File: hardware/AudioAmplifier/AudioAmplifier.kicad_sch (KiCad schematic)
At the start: 7 parts, among them J1 Screw_Terminal_01x02, U1 LM386

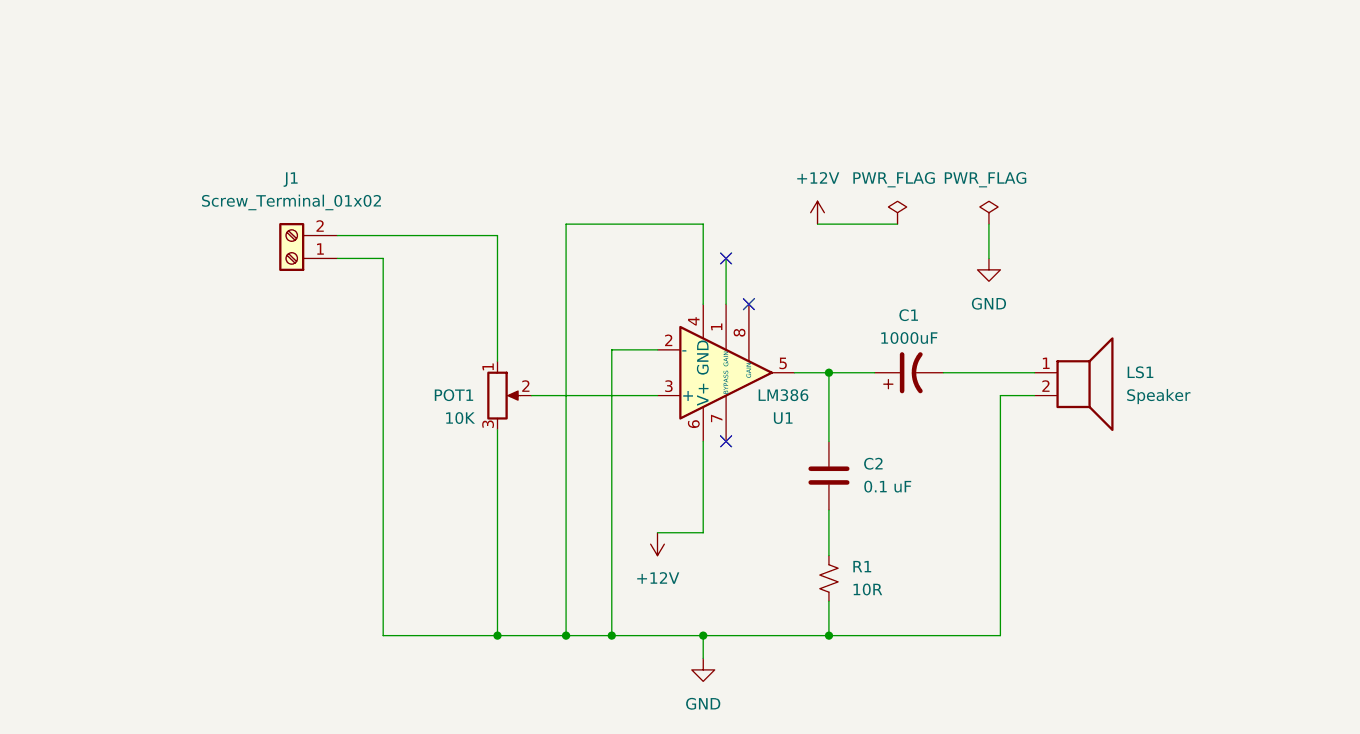
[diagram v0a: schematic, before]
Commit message: Added RC filter into the circuit. Not yet changed THT footprints yet
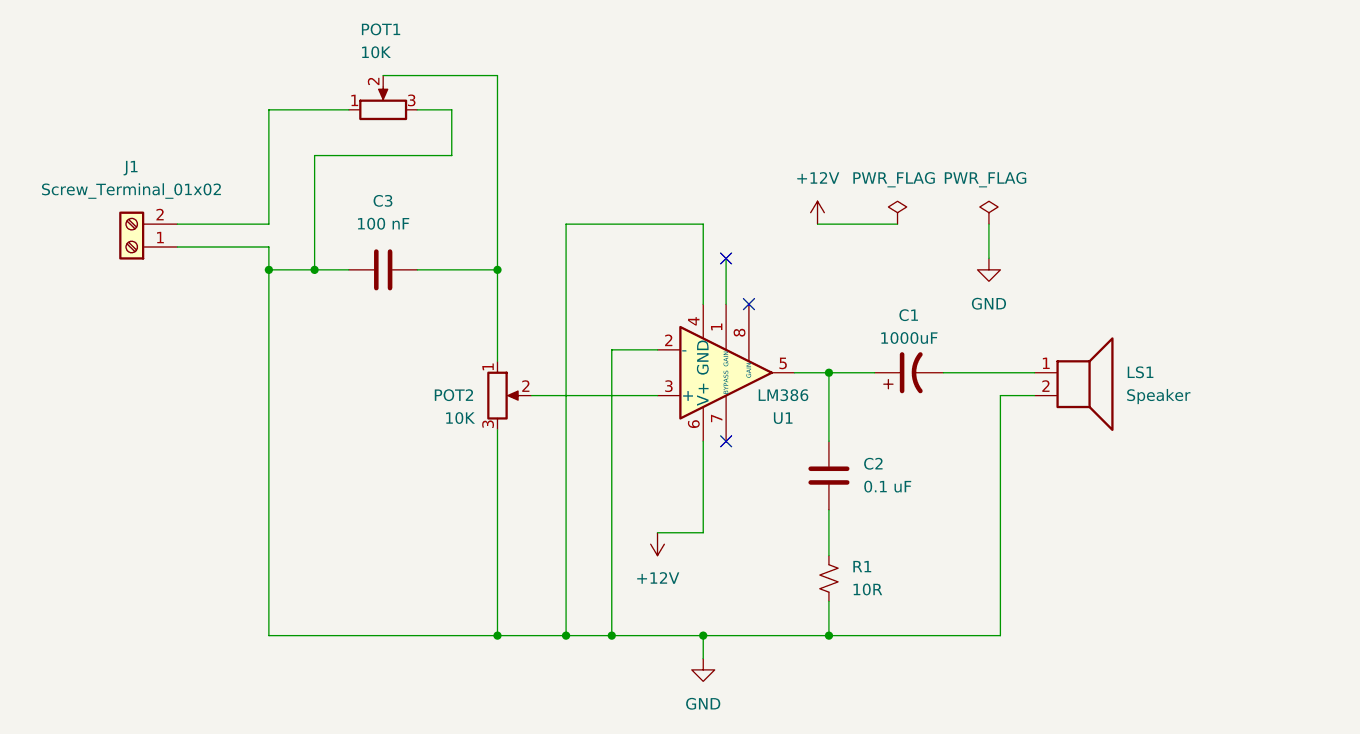
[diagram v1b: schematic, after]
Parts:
- added C3: 100 nF, Capacitor_THT:C_Radial_D4.0mm_H5.0mm_P1.50mm, symbol Device:C
- added POT1: 10K, Potentiometer_THT:Potentiometer_ACP_CA6-H2,5_Horizontal, symbol Device:R_Potentiometer
- C1: footprint Capacitor_THT:C_Radial_D4.0mm_H7.0mm_P1.50mm -> Capacitor_THT:C_Radial_D4.0mm_H5.0mm_P1.50mm
- POT2: renamed from POT1; footprint Potentiometer_THT:Potentiometer_ACP_CA6-H2,5_Horizontal -> Potentiometer_THT:Potentiometer_ACP_CA9-H2,5_Horizontal
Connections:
- net GND: now also C3.1, POT1.3
- net at J1.2 (Pin_2): now also POT1.1; no longer POT2.1
- new net: C3.2, POT1.2, POT2.1
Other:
- moved on the sheet: J1
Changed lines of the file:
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@@
   (junction (at 153.67 97.79) (diameter 0) (color 0 0 0 0)
   )
+  (junction (at 91.44 57.15) (diameter 0) (color 0 0 0 0)
+  )
+  (junction (at 116.84 57.15) (diameter 0) (color 0 0 0 0)
+  )
   (junction (at 129.54 97.79) (diameter 0) (color 0 0 0 0)
   )
@@
   )
   (junction (at 124.46 97.79) (diameter 0) (color 0 0 0 0)
+  )
+  (junction (at 96.52 57.15) (diameter 0) (color 0 0 0 0)
   )
   (no_connect (at 142.24 55.88))
@@
     (stroke (width 0) (type default) (color 0 0 0 0))
   )
+  (wire (pts (xy 91.44 39.37) (xy 100.33 39.37))
+    (stroke (width 0) (type default) (color 0 0 0 0))
+  )
   (wire (pts (xy 176.53 71.12) (xy 172.72 71.12))
     (stroke (width 0) (type default) (color 0 0 0 0))
   )
+  (wire (pts (xy 91.44 57.15) (xy 96.52 57.15))
+    (stroke (width 0) (type default) (color 0 0 0 0))
+  )
+  (wire (pts (xy 96.52 57.15) (xy 100.33 57.15))
+    (stroke (width 0) (type default) (color 0 0 0 0))
+  )
   (wire (pts (xy 153.67 83.82) (xy 153.67 88.9))
     (stroke (width 0) (type default) (color 0 0 0 0))
   )
+  (wire (pts (xy 91.44 54.61) (xy 91.44 57.15))
+    (stroke (width 0) (type default) (color 0 0 0 0))
+  )
+  (wire (pts (xy 116.84 35.56) (xy 116.84 57.15))
+    (stroke (width 0) (type default) (color 0 0 0 0))
+  )
   (wire (pts (xy 116.84 97.79) (xy 124.46 97.79))
     (stroke (width 0) (type default) (color 0 0 0 0))
   )
-  (wire (pts (xy 99.06 55.88) (xy 104.14 55.88))
-    (stroke (width 0) (type default) (color 0 0 0 0))
-  )
-  (wire (pts (xy 104.14 55.88) (xy 104.14 97.79))
+  (wire (pts (xy 81.28 54.61) (xy 91.44 54.61))
     (stroke (width 0) (type default) (color 0 0 0 0))
   )
@@
     (stroke (width 0) (type default) (color 0 0 0 0))
   )
+  (wire (pts (xy 111.76 44.45) (xy 111.76 39.37))
+    (stroke (width 0) (type default) (color 0 0 0 0))
+  )
+  (wire (pts (xy 91.44 52.07) (xy 91.44 39.37))
+    (stroke (width 0) (type default) (color 0 0 0 0))
+  )
+  (wire (pts (xy 91.44 57.15) (xy 91.44 97.79))
+    (stroke (width 0) (type default) (color 0 0 0 0))
+  )
   (wire (pts (xy 129.54 97.79) (xy 139.7 97.79))
     (stroke (width 0) (type default) (color 0 0 0 0))
   )
+  (wire (pts (xy 96.52 57.15) (xy 96.52 44.45))
+    (stroke (width 0) (type default) (color 0 0 0 0))
+  )
   (wire (pts (xy 139.7 97.79) (xy 139.7 100.33))
     (stroke (width 0) (type default) (color 0 0 0 0))
@@
     (stroke (width 0) (type default) (color 0 0 0 0))
   )
-  (wire (pts (xy 99.06 53.34) (xy 116.84 53.34))
+  (wire (pts (xy 107.95 57.15) (xy 116.84 57.15))
     (stroke (width 0) (type default) (color 0 0 0 0))
   )
@@
     (stroke (width 0) (type default) (color 0 0 0 0))
   )
-  (wire (pts (xy 104.14 97.79) (xy 116.84 97.79))
+  (wire (pts (xy 81.28 52.07) (xy 91.44 52.07))
+    (stroke (width 0) (type default) (color 0 0 0 0))
+  )
+  (wire (pts (xy 91.44 97.79) (xy 116.84 97.79))
     (stroke (width 0) (type default) (color 0 0 0 0))
   )
@@
     (stroke (width 0) (type default) (color 0 0 0 0))
   )
+  (wire (pts (xy 104.14 35.56) (xy 116.84 35.56))
+    (stroke (width 0) (type default) (color 0 0 0 0))
+  )
   (wire (pts (xy 172.72 71.12) (xy 172.72 97.79))
     (stroke (width 0) (type default) (color 0 0 0 0))
@@
     (stroke (width 0) (type default) (color 0 0 0 0))
   )
-  (wire (pts (xy 116.84 53.34) (xy 116.84 67.31))
-    (stroke (width 0) (type default) (color 0 0 0 0))
-  )
   (wire (pts (xy 139.7 86.36) (xy 134.62 86.36))
     (stroke (width 0) (type default) (color 0 0 0 0))
   )
+  (wire (pts (xy 111.76 39.37) (xy 107.95 39.37))
+    (stroke (width 0) (type default) (color 0 0 0 0))
+  )
   (wire (pts (xy 139.7 52.07) (xy 124.46 52.07))
     (stroke (width 0) (type default) (color 0 0 0 0))
@@
     (stroke (width 0) (type default) (color 0 0 0 0))
   )
+  (wire (pts (xy 96.52 44.45) (xy 111.76 44.45))
+    (stroke (width 0) (type default) (color 0 0 0 0))
+  )
   (wire (pts (xy 171.45 52.07) (xy 171.45 55.88))
     (stroke (width 0) (type default) (color 0 0 0 0))
@@
     (stroke (width 0) (type default) (color 0 0 0 0))
   )
+  (wire (pts (xy 116.84 57.15) (xy 116.84 67.31))
+    (stroke (width 0) (type default) (color 0 0 0 0))
+  )
   (wire (pts (xy 153.67 97.79) (xy 172.72 97.79))
     (stroke (width 0) (type default) (color 0 0 0 0))
@@
     (stroke (width 0) (type default) (color 0 0 0 0))
   )
-  (symbol (lib_id "Connector:Screw_Terminal_01x02") (at 93.98 55.88 180) (unit 1)
-    (in_bom yes) (on_board yes) (fields_autoplaced)
-    (property "Reference" "J1" (id 0) (at 93.98 46.99 0))
-    (property "Value" "Screw_Terminal_01x02" (id 1) (at 93.98 49.53 0))
-    (property "Footprint" "TerminalBlock_Phoenix:TerminalBlock_Phoenix_MKDS-1,5-2-5.08_1x02_P5.08mm_Horizontal" (id 2) (at 93.98 55.88 0)
-      (effects (font (size 1.27 1.27)) hide)
-    )
-    (property "Datasheet" "~" (id 3) (at 93.98 55.88 0)
+  (symbol (lib_id "Connector:Screw_Terminal_01x02") (at 76.2 54.61 180) (unit 1)
+    (in_bom yes) (on_board yes) (fields_autoplaced)
+    (property "Reference" "J1" (id 0) (at 76.2 45.72 0))
+    (property "Value" "Screw_Terminal_01x02" (id 1) (at 76.2 48.26 0))
+    (property "Footprint" "TerminalBlock_Phoenix:TerminalBlock_Phoenix_MKDS-1,5-2-5.08_1x02_P5.08mm_Horizontal" (id 2) (at 76.2 54.61 0)
+      (effects (font (size 1.27 1.27)) hide)
+    )
+    (property "Datasheet" "~" (id 3) (at 76.2 54.61 0)
       (effects (font (size 1.27 1.27)) hide)
     )
@@
   (symbol (lib_id "Device:R_Potentiometer") (at 116.84 71.12 0) (unit 1)
     (in_bom yes) (on_board yes)
-    (property "Reference" "POT1" (id 0) (at 114.3 71.12 0)
+    (property "Reference" "POT2" (id 0) (at 114.3 71.12 0)
       (effects (font (size 1.27 1.27)) (justify right))
     )
@@
       (effects (font (size 1.27 1.27)) (justify right))
     )
-    (property "Footprint" "Potentiometer_THT:Potentiometer_ACP_CA6-H2,5_Horizontal" (id 2) (at 116.84 71.12 0)
+    (property "Footprint" "Potentiometer_THT:Potentiometer_ACP_CA9-H2,5_Horizontal" (id 2) (at 116.84 71.12 0)
       (effects (font (size 1.27 1.27)) hide)
     )
@@
     (property "Reference" "C1" (id 0) (at 162.56 62.23 90))
     (property "Value" "1000uF" (id 1) (at 162.56 64.77 90))
-    (property "Footprint" "Capacitor_THT:C_Radial_D4.0mm_H7.0mm_P1.50mm" (id 2) (at 162.56 68.58 0)
+    (property "Footprint" "Capacitor_THT:C_Radial_D4.0mm_H5.0mm_P1.50mm" (id 2) (at 162.56 68.58 0)
       (effects (font (size 1.27 1.27)) hide)
     )
@@
     )
     (pin "1")
+  )
+  (symbol (lib_id "Device:C") (at 104.14 57.15 90) (unit 1)
+    (in_bom yes) (on_board yes) (fields_autoplaced)
+    (property "Reference" "C3" (id 0) (at 104.14 49.53 90))
+    (property "Value" "100 nF" (id 1) (at 104.14 52.07 90))
+    (property "Footprint" "Capacitor_THT:C_Radial_D4.0mm_H5.0mm_P1.50mm" (id 2) (at 107.95 56.1848 0)
+      (effects (font (size 1.27 1.27)) hide)
+    )
+    (property "Datasheet" "~" (id 3) (at 104.14 57.15 0)
+      (effects (font (size 1.27 1.27)) hide)
+    )
+    (pin "1")
+    (pin "2")
+  )
+  (symbol (lib_id "Device:R_Potentiometer") (at 104.14 39.37 90) (unit 1)
+    (in_bom yes) (on_board yes)
+    (property "Reference" "POT1" (id 0) (at 101.6 30.48 90)
+      (effects (font (size 1.27 1.27)) (justify right))
+    )
+    (property "Value" "10K" (id 1) (at 101.6 33.02 90)
+      (effects (font (size 1.27 1.27)) (justify right))
+    )
+    (property "Footprint" "Potentiometer_THT:Potentiometer_ACP_CA6-H2,5_Horizontal" (id 2) (at 104.14 39.37 0)
+      (effects (font (size 1.27 1.27)) hide)
+    )
+    (property "Datasheet" "~" (id 3) (at 104.14 39.37 0)
+      (effects (font (size 1.27 1.27)) hide)
+    )
+    (pin "1")
+    (pin "2")
+    (pin "3")
   )
   (symbol (lib_id "power:GND") (at 171.45 55.88 0) (unit 1)
@@
     )
     (path "/5f93ca8c-4e9c-4d7a-b328-844876fcf208"
-      (reference "C1") (unit 1) (value "1000uF") (footprint "Capacitor_THT:C_Radial_D4.0mm_H7.0mm_P1.50mm")
+      (reference "C1") (unit 1) (value "1000uF") (footprint "Capacitor_THT:C_Radial_D4.0mm_H5.0mm_P1.50mm")
     )
     (path "/8e53c0ce-459b-49bb-8303-7edcde4bf1f1"
       (reference "C2") (unit 1) (value "0.1 uF") (footprint "Capacitor_THT:C_Radial_D4.0mm_H5.0mm_P1.50mm")
     )
+    (path "/ceffba6a-2877-4199-9b56-4e2f0159df47"
+      (reference "C3") (unit 1) (value "100 nF") (footprint "Capacitor_THT:C_Radial_D4.0mm_H5.0mm_P1.50mm")
+    )
     (path "/1370d0e0-9eea-4151-b9e4-0d4babdd9dd4"
       (reference "J1") (unit 1) (value "Screw_Terminal_01x02") (footprint "TerminalBlock_Phoenix:TerminalBlock_Phoenix_MKDS-1,5-2-5.08_1x02_P5.08mm_Horizontal")
@@
       (reference "LS1") (unit 1) (value "Speaker") (footprint "Buzzer_Beeper:Buzzer_12x9.5RM7.6")
     )
+    (path "/d64e0cf6-40fe-458d-ac94-89f5f9d15ec9"
+      (reference "POT1") (unit 1) (value "10K") (footprint "Potentiometer_THT:Potentiometer_ACP_CA6-H2,5_Horizontal")
+    )
     (path "/3af71a2d-c886-4241-b6ca-f5d2b2f9469e"
-      (reference "POT1") (unit 1) (value "10K") (footprint "Potentiometer_THT:Potentiometer_ACP_CA6-H2,5_Horizontal")
+      (reference "POT2") (unit 1) (value "10K") (footprint "Potentiometer_THT:Potentiometer_ACP_CA9-H2,5_Horizontal")
     )
     (path "/586e7c98-abd2-4ec7-a193-93b587446b80"

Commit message: Added ground plain and increased track size, changed capacitor size
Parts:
- removed LS1: Speaker, Buzzer_Beeper:Buzzer_12x9.5RM7.6, symbol Device:Speaker
- added C4: 4.7uF, Capacitor_THT:C_Disc_D3.8mm_W2.6mm_P2.50mm, symbol Device:C
- added J2: Screw_Terminal_01x02, TerminalBlock_Phoenix:TerminalBlock_Phoenix_MKDS-1,5-2-5.08_1x02_P5.08mm_Horizontal, symbol Connector:Screw_Terminal_01x02
- C1: footprint Capacitor_THT:C_Radial_D4.0mm_H5.0mm_P1.50mm -> Capacitor_THT:CP_Radial_D10.0mm_P2.50mm
- C3: footprint Capacitor_THT:C_Radial_D4.0mm_H5.0mm_P1.50mm -> Capacitor_THT:C_Radial_D6.3mm_H5.0mm_P2.50mm
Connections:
- net GND: now also J2.2 (Pin_2)
- net at J1.2 (Pin_2): now also C4.2; no longer POT1.1
- net at C1.2: now also J2.1 (Pin_1)
- new net: C4.1, POT1.1
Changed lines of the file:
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@@
   (junction (at 91.44 57.15) (diameter 0) (color 0 0 0 0)
   )
+  (junction (at 97.79 57.15) (diameter 0) (color 0 0 0 0)
+  )
   (junction (at 116.84 57.15) (diameter 0) (color 0 0 0 0)
   )
@@
   )
   (junction (at 124.46 97.79) (diameter 0) (color 0 0 0 0)
-  )
-  (junction (at 96.52 57.15) (diameter 0) (color 0 0 0 0)
   )
   (no_connect (at 142.24 55.88))
@@
     (stroke (width 0) (type default) (color 0 0 0 0))
   )
+  (wire (pts (xy 91.44 49.53) (xy 91.44 52.07))
+    (stroke (width 0) (type default) (color 0 0 0 0))
+  )
   (wire (pts (xy 124.46 97.79) (xy 129.54 97.79))
     (stroke (width 0) (type default) (color 0 0 0 0))
@@
     (stroke (width 0) (type default) (color 0 0 0 0))
   )
-  (wire (pts (xy 176.53 71.12) (xy 172.72 71.12))
-    (stroke (width 0) (type default) (color 0 0 0 0))
-  )
-  (wire (pts (xy 91.44 57.15) (xy 96.52 57.15))
-    (stroke (width 0) (type default) (color 0 0 0 0))
-  )
-  (wire (pts (xy 96.52 57.15) (xy 100.33 57.15))
+  (wire (pts (xy 172.72 71.12) (xy 177.8 71.12))
     (stroke (width 0) (type default) (color 0 0 0 0))
   )
@@
     (stroke (width 0) (type default) (color 0 0 0 0))
   )
+  (wire (pts (xy 91.44 39.37) (xy 91.44 41.91))
+    (stroke (width 0) (type default) (color 0 0 0 0))
+  )
   (wire (pts (xy 120.65 71.12) (xy 134.62 71.12))
     (stroke (width 0) (type default) (color 0 0 0 0))
@@
     (stroke (width 0) (type default) (color 0 0 0 0))
   )
-  (wire (pts (xy 91.44 52.07) (xy 91.44 39.37))
-    (stroke (width 0) (type default) (color 0 0 0 0))
-  )
   (wire (pts (xy 91.44 57.15) (xy 91.44 97.79))
     (stroke (width 0) (type default) (color 0 0 0 0))
@@
     (stroke (width 0) (type default) (color 0 0 0 0))
   )
-  (wire (pts (xy 96.52 57.15) (xy 96.52 44.45))
+  (wire (pts (xy 97.79 57.15) (xy 97.79 44.45))
     (stroke (width 0) (type default) (color 0 0 0 0))
   )
@@
     (stroke (width 0) (type default) (color 0 0 0 0))
   )
-  (wire (pts (xy 96.52 44.45) (xy 111.76 44.45))
+  (wire (pts (xy 97.79 44.45) (xy 111.76 44.45))
     (stroke (width 0) (type default) (color 0 0 0 0))
   )
@@
     (stroke (width 0) (type default) (color 0 0 0 0))
   )
+  (wire (pts (xy 97.79 57.15) (xy 100.33 57.15))
+    (stroke (width 0) (type default) (color 0 0 0 0))
+  )
   (wire (pts (xy 129.54 66.04) (xy 129.54 97.79))
     (stroke (width 0) (type default) (color 0 0 0 0))
@@
     (stroke (width 0) (type default) (color 0 0 0 0))
   )
-  (wire (pts (xy 166.37 68.58) (xy 176.53 68.58))
+  (wire (pts (xy 166.37 68.58) (xy 177.8 68.58))
     (stroke (width 0) (type default) (color 0 0 0 0))
   )
   (wire (pts (xy 139.7 76.2) (xy 139.7 86.36))
+    (stroke (width 0) (type default) (color 0 0 0 0))
+  )
+  (wire (pts (xy 91.44 57.15) (xy 97.79 57.15))
     (stroke (width 0) (type default) (color 0 0 0 0))
   )
@@
     (pin "2")
   )
-  (symbol (lib_id "Device:Speaker") (at 181.61 68.58 0) (unit 1)
-    (in_bom yes) (on_board yes) (fields_autoplaced)
-    (property "Reference" "LS1" (id 0) (at 186.69 68.5799 0)
-      (effects (font (size 1.27 1.27)) (justify left))
-    )
-    (property "Value" "Speaker" (id 1) (at 186.69 71.1199 0)
-      (effects (font (size 1.27 1.27)) (justify left))
-    )
-    (property "Footprint" "Buzzer_Beeper:Buzzer_12x9.5RM7.6" (id 2) (at 181.61 73.66 0)
-      (effects (font (size 1.27 1.27)) hide)
-    )
-    (property "Datasheet" "~" (id 3) (at 181.356 69.85 0)
-      (effects (font (size 1.27 1.27)) hide)
-    )
-    (pin "1")
-    (pin "2")
-  )
   (symbol (lib_id "power:+12V") (at 152.4 52.07 0) (unit 1)
     (in_bom yes) (on_board yes) (fields_autoplaced)
@@
     (property "Reference" "C1" (id 0) (at 162.56 62.23 90))
     (property "Value" "1000uF" (id 1) (at 162.56 64.77 90))
-    (property "Footprint" "Capacitor_THT:C_Radial_D4.0mm_H5.0mm_P1.50mm" (id 2) (at 162.56 68.58 0)
+    (property "Footprint" "Capacitor_THT:CP_Radial_D10.0mm_P2.50mm" (id 2) (at 162.56 68.58 0)
       (effects (font (size 1.27 1.27)) hide)
     )
@@
     )
     (property "Datasheet" "~" (id 3) (at 153.67 80.01 0)
+      (effects (font (size 1.27 1.27)) hide)
+    )
+    (pin "1")
+    (pin "2")
+  )
+  (symbol (lib_id "Connector:Screw_Terminal_01x02") (at 182.88 68.58 0) (unit 1)
+    (in_bom yes) (on_board yes) (fields_autoplaced)
+    (property "Reference" "J2" (id 0) (at 185.42 68.5799 0)
+      (effects (font (size 1.27 1.27)) (justify left))
+    )
+    (property "Value" "Screw_Terminal_01x02" (id 1) (at 185.42 71.1199 0)
+      (effects (font (size 1.27 1.27)) (justify left))
+    )
+    (property "Footprint" "TerminalBlock_Phoenix:TerminalBlock_Phoenix_MKDS-1,5-2-5.08_1x02_P5.08mm_Horizontal" (id 2) (at 182.88 68.58 0)
+      (effects (font (size 1.27 1.27)) hide)
+    )
+    (property "Datasheet" "~" (id 3) (at 182.88 68.58 0)
       (effects (font (size 1.27 1.27)) hide)
     )
@@
     (property "Reference" "C3" (id 0) (at 104.14 49.53 90))
     (property "Value" "100 nF" (id 1) (at 104.14 52.07 90))
-    (property "Footprint" "Capacitor_THT:C_Radial_D4.0mm_H5.0mm_P1.50mm" (id 2) (at 107.95 56.1848 0)
+    (property "Footprint" "Capacitor_THT:C_Radial_D6.3mm_H5.0mm_P2.50mm" (id 2) (at 107.95 56.1848 0)
       (effects (font (size 1.27 1.27)) hide)
     )
@@
     (pin "2")
     (pin "3")
+  )
+  (symbol (lib_id "Device:C") (at 91.44 45.72 0) (unit 1)
+    (in_bom yes) (on_board yes)
+    (property "Reference" "C4" (id 0) (at 87.63 41.91 0)
+      (effects (font (size 1.27 1.27)) (justify left))
+    )
+    (property "Value" "4.7uF" (id 1) (at 95.25 48.26 90)
+      (effects (font (size 1.27 1.27)) (justify left))
+    )
+    (property "Footprint" "Capacitor_THT:C_Disc_D3.8mm_W2.6mm_P2.50mm" (id 2) (at 92.4052 49.53 0)
+      (effects (font (size 1.27 1.27)) hide)
+    )
+    (property "Datasheet" "~" (id 3) (at 91.44 45.72 0)
+      (effects (font (size 1.27 1.27)) hide)
+    )
+    (pin "1")
+    (pin "2")
   )
   (symbol (lib_id "power:GND") (at 171.45 55.88 0) (unit 1)
@@
     )
     (path "/5f93ca8c-4e9c-4d7a-b328-844876fcf208"
-      (reference "C1") (unit 1) (value "1000uF") (footprint "Capacitor_THT:C_Radial_D4.0mm_H5.0mm_P1.50mm")
+      (reference "C1") (unit 1) (value "1000uF") (footprint "Capacitor_THT:CP_Radial_D10.0mm_P2.50mm")
     )
     (path "/8e53c0ce-459b-49bb-8303-7edcde4bf1f1"
@@
     )
     (path "/ceffba6a-2877-4199-9b56-4e2f0159df47"
-      (reference "C3") (unit 1) (value "100 nF") (footprint "Capacitor_THT:C_Radial_D4.0mm_H5.0mm_P1.50mm")
+      (reference "C3") (unit 1) (value "100 nF") (footprint "Capacitor_THT:C_Radial_D6.3mm_H5.0mm_P2.50mm")
+    )
+    (path "/d9fa713c-3a85-42f1-a9f2-ff815d600e4c"
+      (reference "C4") (unit 1) (value "4.7uF") (footprint "Capacitor_THT:C_Disc_D3.8mm_W2.6mm_P2.50mm")
     )
     (path "/1370d0e0-9eea-4151-b9e4-0d4babdd9dd4"
       (reference "J1") (unit 1) (value "Screw_Terminal_01x02") (footprint "TerminalBlock_Phoenix:TerminalBlock_Phoenix_MKDS-1,5-2-5.08_1x02_P5.08mm_Horizontal")
     )
-    (path "/1bcf4c4f-678c-486a-9199-d33e2a6c7932"
-      (reference "LS1") (unit 1) (value "Speaker") (footprint "Buzzer_Beeper:Buzzer_12x9.5RM7.6")
+    (path "/9b1bb401-a68c-4635-a33a-da734000841d"
+      (reference "J2") (unit 1) (value "Screw_Terminal_01x02") (footprint "TerminalBlock_Phoenix:TerminalBlock_Phoenix_MKDS-1,5-2-5.08_1x02_P5.08mm_Horizontal")
     )
     (path "/d64e0cf6-40fe-458d-ac94-89f5f9d15ec9"
